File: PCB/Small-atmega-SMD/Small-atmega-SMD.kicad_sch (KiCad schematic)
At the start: 30 parts, among them J1 Daisy port in, J2 ICSP_ISP6, J3 UART, J4 Daisy port out, K1 HYC77-TF09-200, U1 PC817C-S, U2 SE5218, U21 TXB0104QPWRQ1, U3 ATmega328P-AU, Y1 16MHz

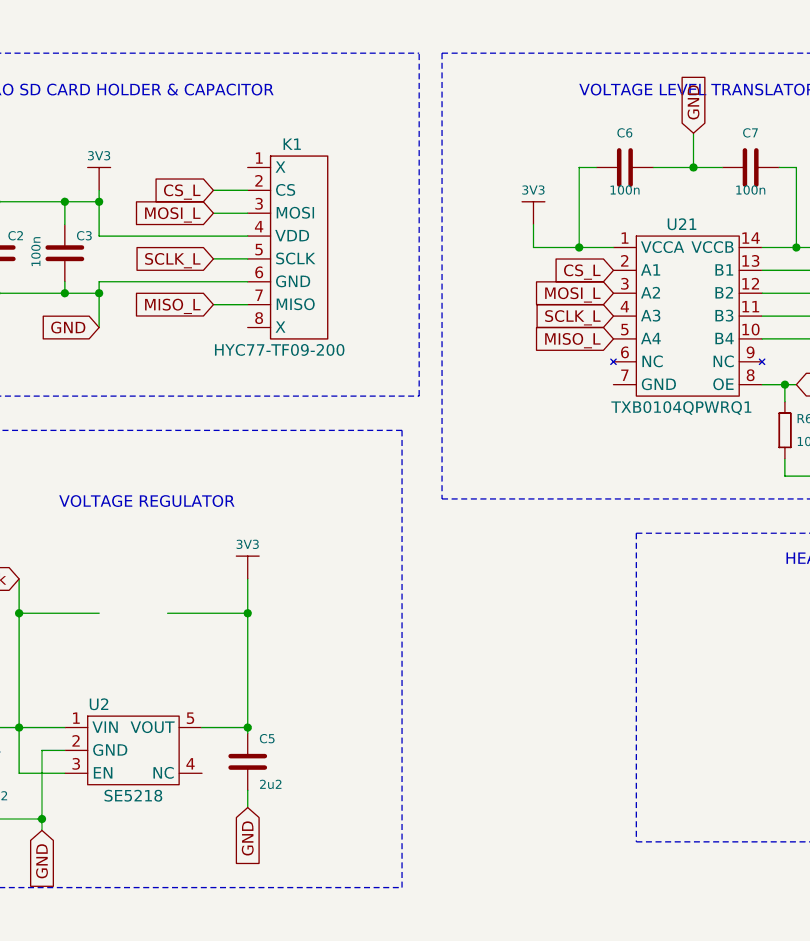
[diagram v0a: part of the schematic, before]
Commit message: Add GND to level shifter :-/
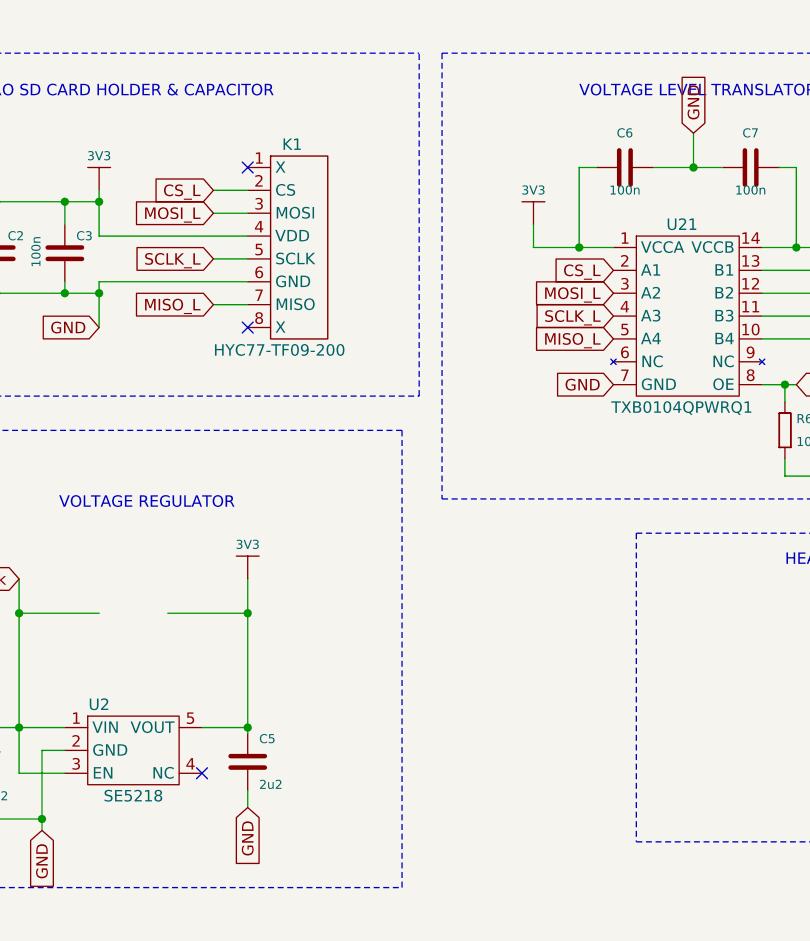
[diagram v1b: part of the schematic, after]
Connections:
- net GND: now also U21.7 (GND)
- no-connect marks 5 -> 8
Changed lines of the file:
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@@
+	)
+	(no_connect
+		(at -91.44 49.53)
 	)
 	(no_connect
@@
 	)
 	(no_connect
+		(at -96.52 99.06)
+	)
+	(no_connect
+		(at -91.44 31.75)
+	)
+	(no_connect
 		(at 27.94 44.45)
 	)
@@
 				(hide yes)
 			)
+		)
+	)
+	(global_label "GND"
+		(shape input)
+		(at -50.8 55.88 180)
+		(fields_autoplaced yes)
+		(effects
+			(font
+				(size 1.27 1.27)
+			)
+			(justify right)
+		)
+		(property "Intersheetrefs" "${INTERSHEET_REFS}"
+			(at -57.6557 55.88 0)
+			(effects
+				(font
+					(size 1.27 1.27)
+				)
+				(justify right)
+				(hide yes)
+			)
